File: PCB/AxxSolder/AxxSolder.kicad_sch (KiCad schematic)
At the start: 93 parts, among them IC1 LTC4440AHMS8E-5#PBF, IC2 STM32G431KBT6, IC3 TMP236AQDBZRQ1, IC4 OPA2333AIDRBR, IC5 STM32G431KBT6, IC6 TPS54302DDCR, J1 Conn_01x07_Male, J4 Conn_01x07_Male, Q2 2N7002NXAKR, U1 PEC11L-4220F-S0015, U2 BSC014N04LS

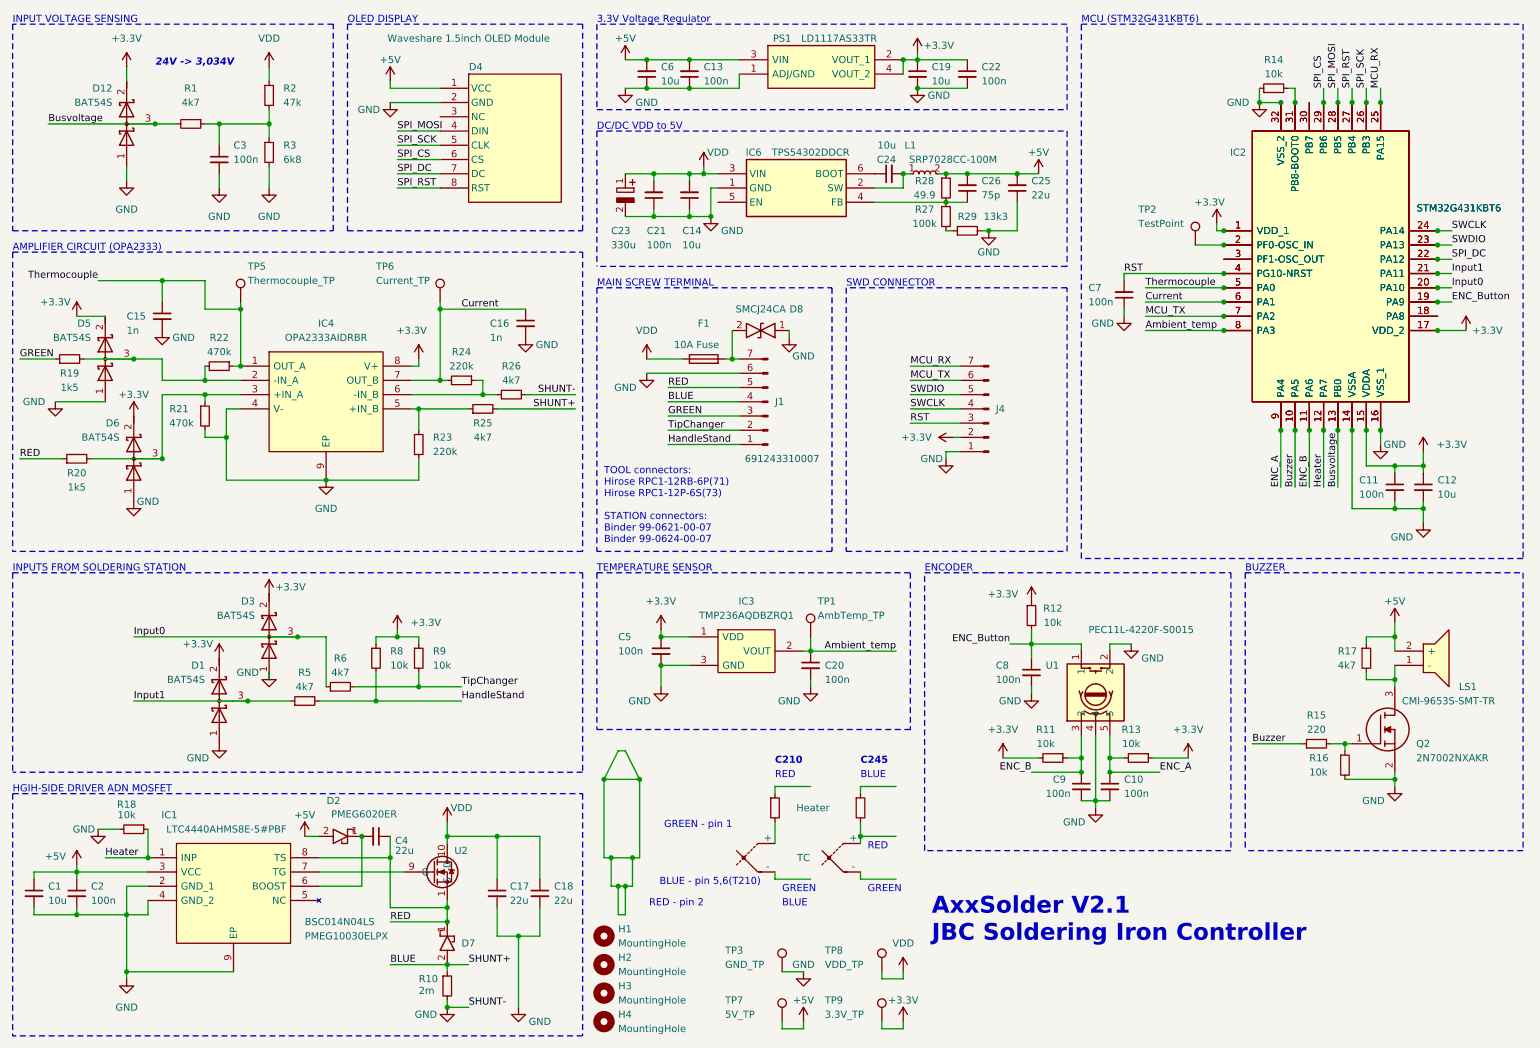
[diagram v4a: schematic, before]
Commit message: Update schematic to reflect new naming of inputs, Stand_inp and Handle_inp
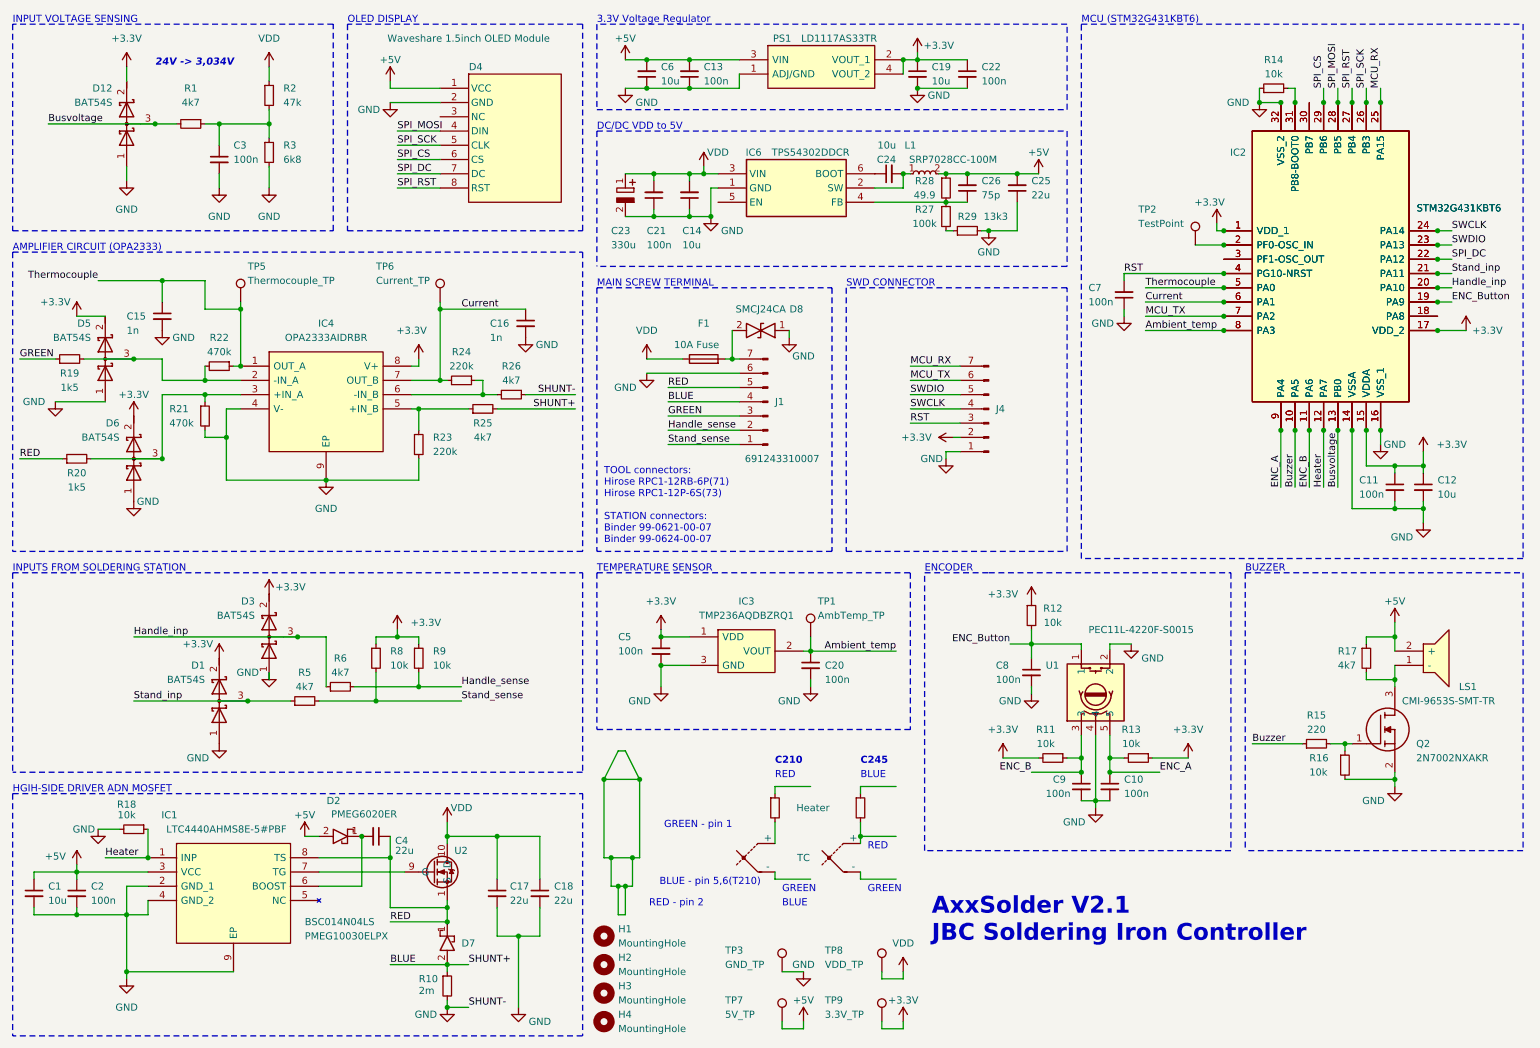
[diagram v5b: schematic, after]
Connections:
- net HandleStand renamed Stand_sense
- net Input0 renamed Handle_inp
- net Input1 renamed Stand_inp
- net TipChanger renamed Handle_sense
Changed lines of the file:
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@@
     (effects (font (size 1.27 1.27)) (justify left bottom))
   )
-  (label "Input0" (at 35.56 125.73 0) (fields_autoplaced)
+  (label "Stand_inp" (at 35.56 137.16 0) (fields_autoplaced)
     (effects (font (size 1.27 1.27)) (justify left bottom))
   )
@@
     (effects (font (size 1.27 1.27)) (justify left bottom))
   )
-  (label "HandleStand" (at 130.81 91.44 0) (fields_autoplaced)
+  (label "Handle_sense" (at 130.81 88.9 0) (fields_autoplaced)
     (effects (font (size 1.27 1.27)) (justify left bottom))
   )
@@
     (effects (font (size 1.27 1.27)) (justify left bottom))
   )
-  (label "Input1" (at 270.51 60.96 0) (fields_autoplaced)
+  (label "Handle_inp" (at 270.51 63.5 0) (fields_autoplaced)
     (effects (font (size 1.27 1.27)) (justify left bottom))
   )
@@
     (effects (font (size 1.27 1.27)) (justify left bottom))
   )
-  (label "TipChanger" (at 130.81 88.9 0) (fields_autoplaced)
+  (label "Stand_sense" (at 130.81 91.44 0) (fields_autoplaced)
     (effects (font (size 1.27 1.27)) (justify left bottom))
   )
@@
     (effects (font (size 1.27 1.27)) (justify left bottom))
   )
-  (label "TipChanger" (at 93.98 134.62 0) (fields_autoplaced)
+  (label "Stand_sense" (at 93.98 137.16 0) (fields_autoplaced)
     (effects (font (size 1.27 1.27)) (justify left bottom))
   )
@@
     (effects (font (size 1.27 1.27)) (justify left bottom))
   )
-  (label "Input1" (at 35.56 137.16 0) (fields_autoplaced)
+  (label "Handle_inp" (at 35.56 125.73 0) (fields_autoplaced)
     (effects (font (size 1.27 1.27)) (justify left bottom))
   )
@@
     (effects (font (size 1.27 1.27)) (justify left bottom))
   )
-  (label "Input0" (at 270.51 63.5 0) (fields_autoplaced)
+  (label "Stand_inp" (at 270.51 60.96 0) (fields_autoplaced)
     (effects (font (size 1.27 1.27)) (justify left bottom))
   )
@@
     (effects (font (size 1.27 1.27)) (justify left bottom))
   )
-  (label "HandleStand" (at 93.98 137.16 0) (fields_autoplaced)
+  (label "Handle_sense" (at 93.98 134.62 0) (fields_autoplaced)
     (effects (font (size 1.27 1.27)) (justify left bottom))
   )

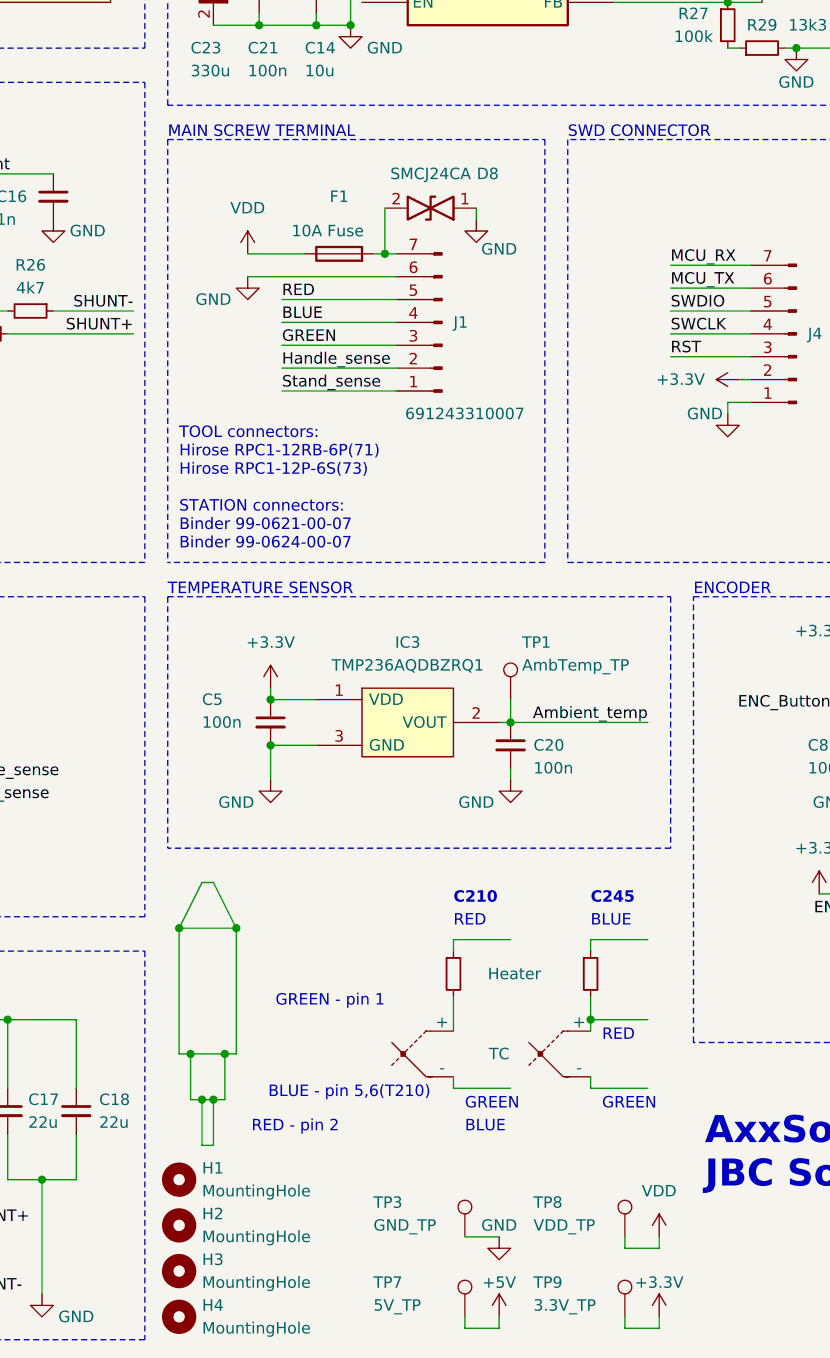
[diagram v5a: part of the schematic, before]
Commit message: Update schematic with proper connections
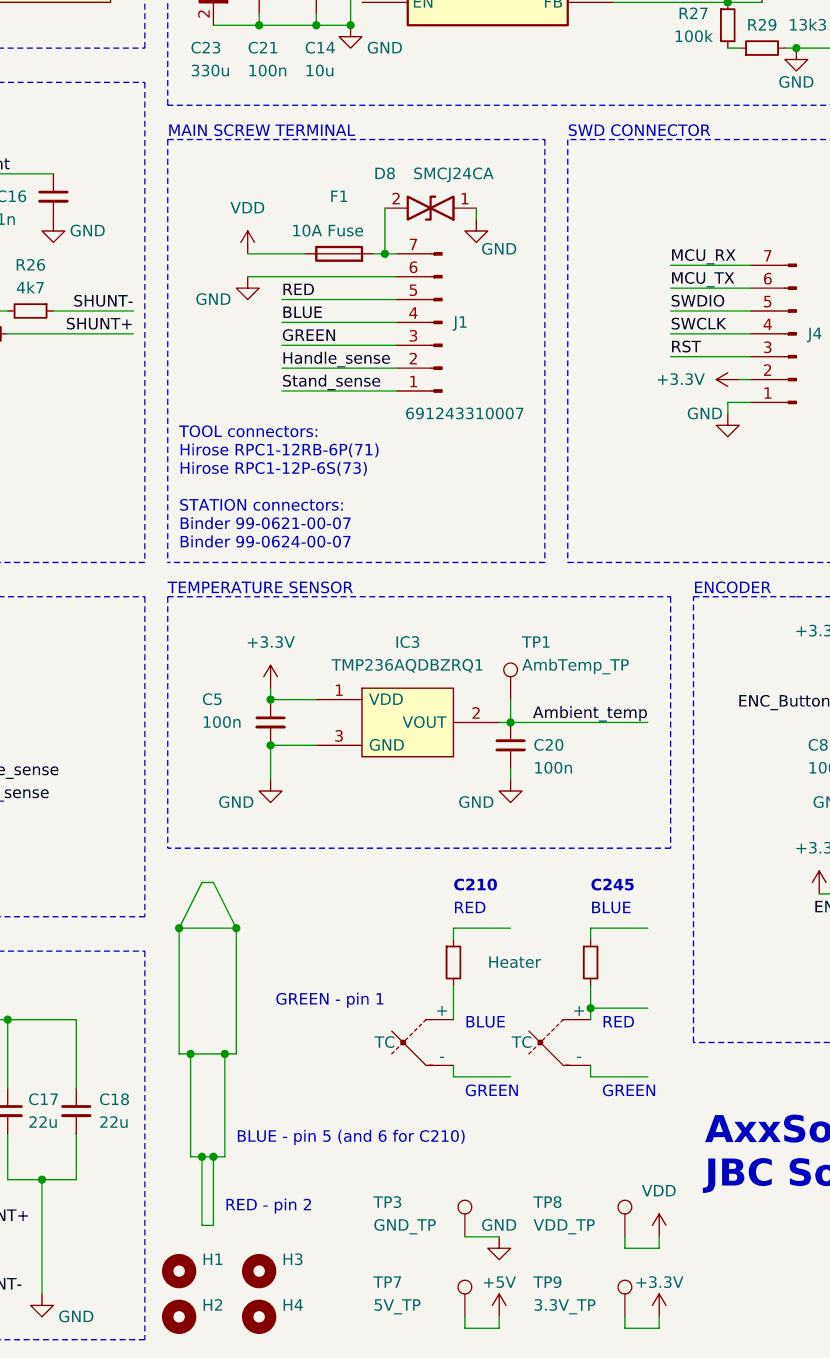
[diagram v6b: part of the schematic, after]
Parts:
- TC2: value Thermocouple -> TC
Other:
- note added: "BLUE - pin 5 (and 6 for C210)"
- note removed: "BLUE - pin 5,6(T210)"
- moved on the sheet: H1, H2, H3, H4

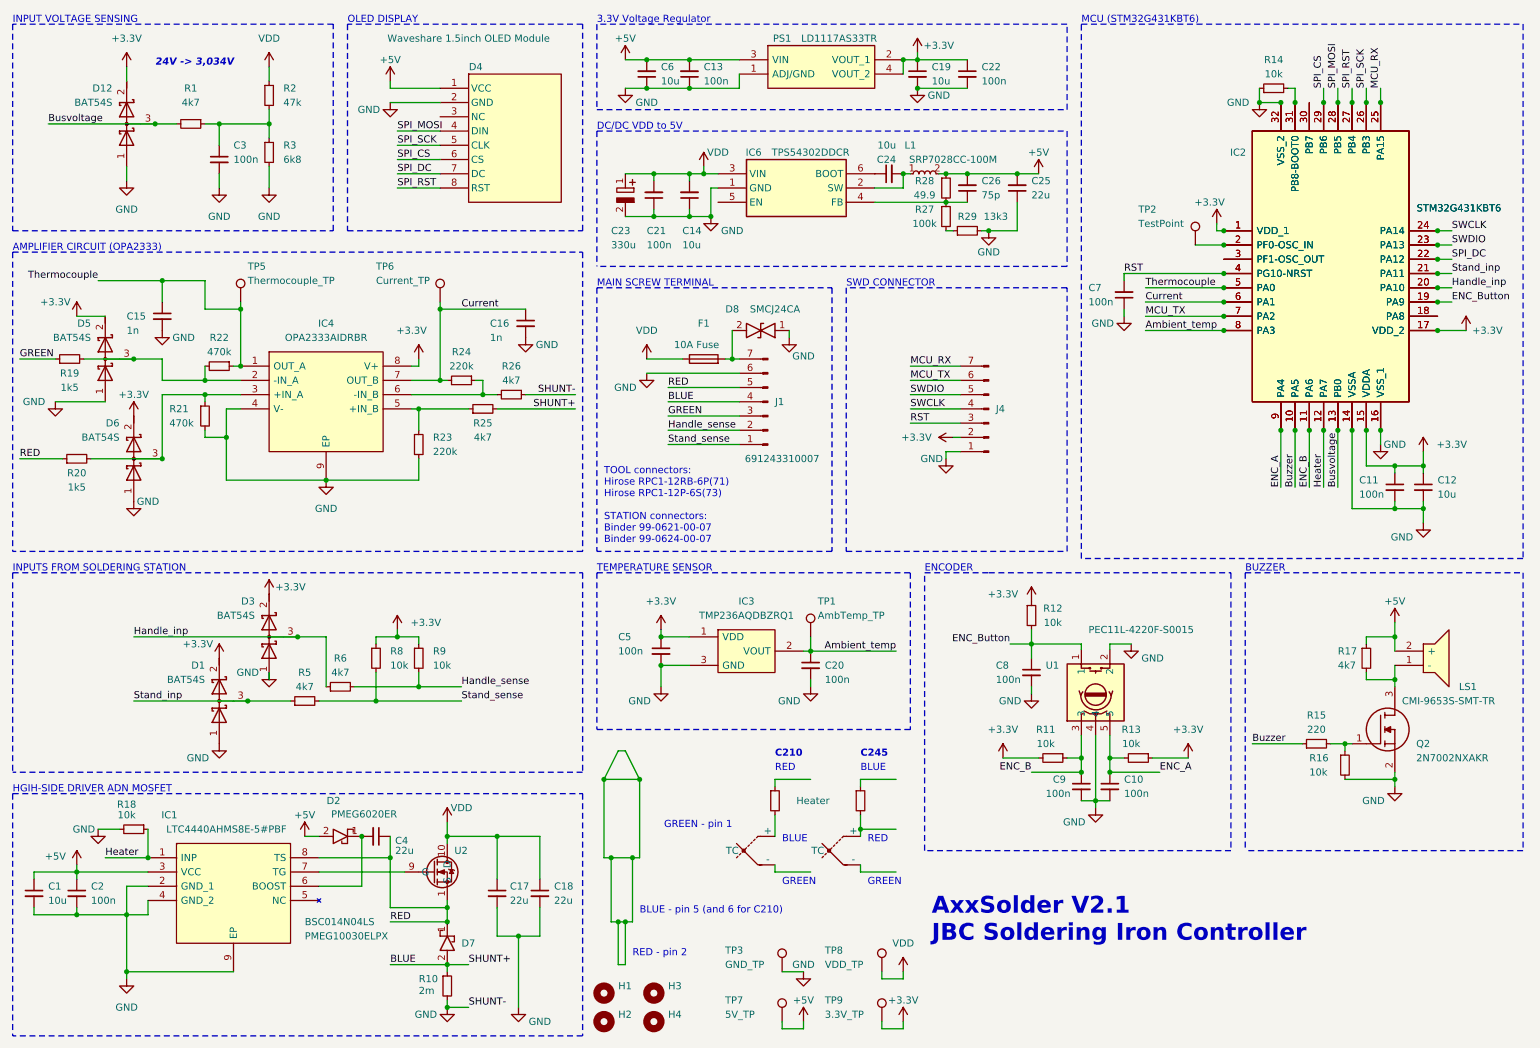
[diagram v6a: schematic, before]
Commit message: Fix output voltage from DC/DC by switching values of R28 and R27. Also change value of C24
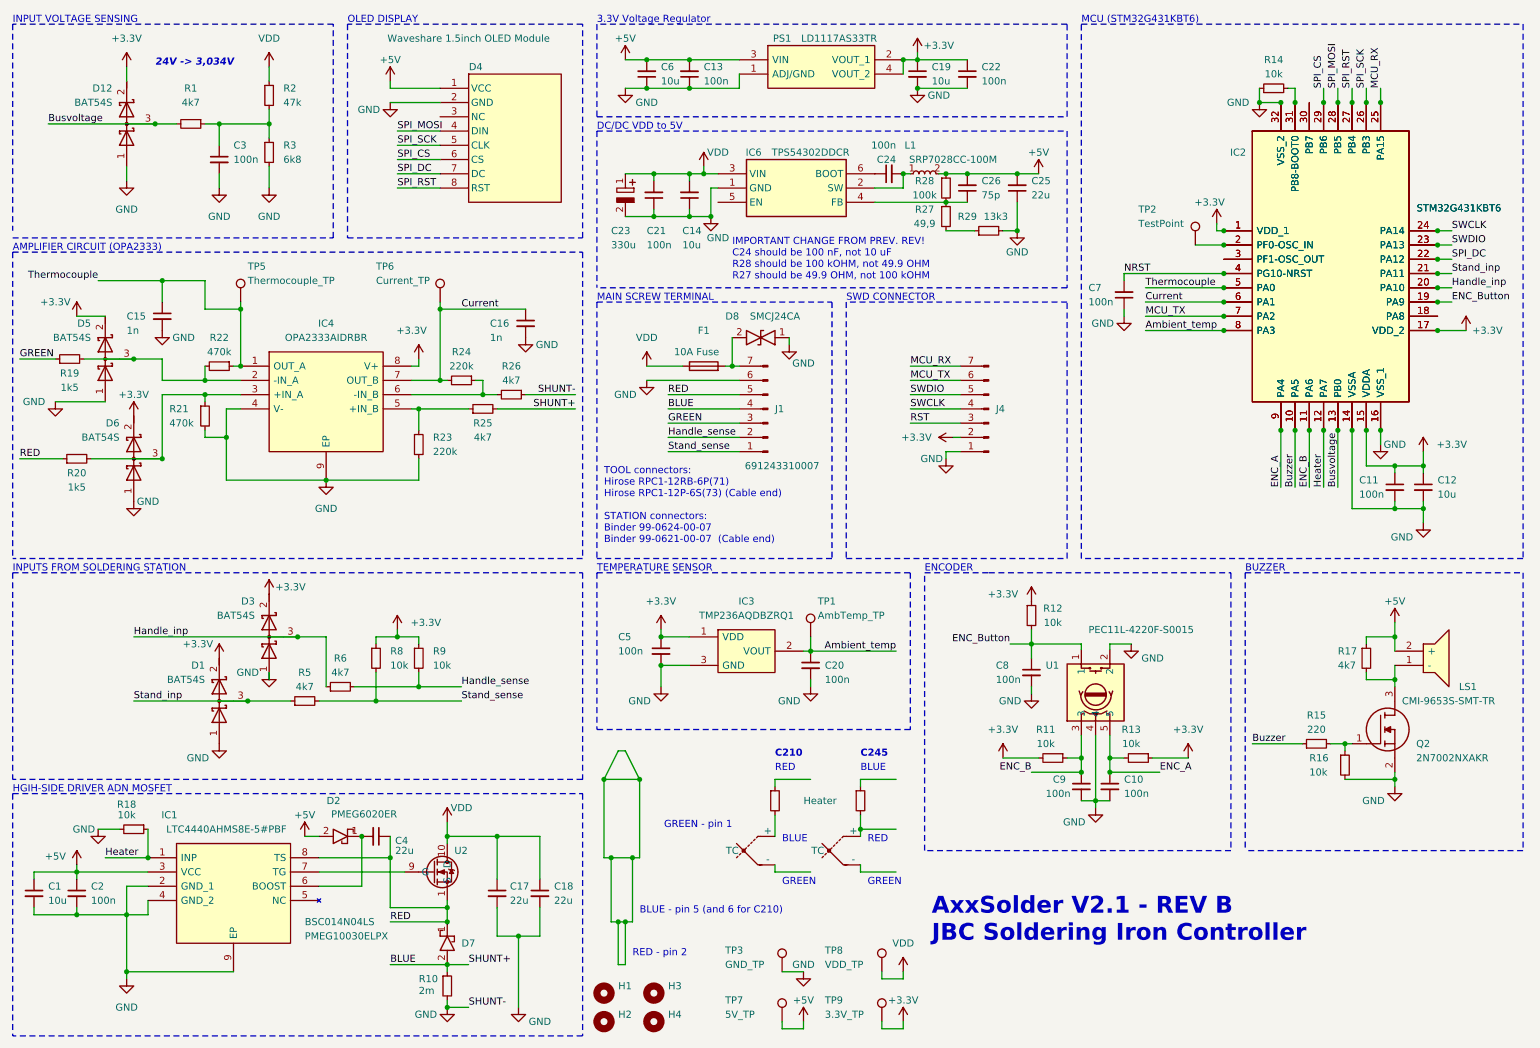
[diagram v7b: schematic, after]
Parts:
- C24: value 10u -> 100n
- R27: value 100k -> 49,9
- R28: value 49.9 -> 100k
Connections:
- net RST: no longer C7.2, IC2.4 (PG10-NRST), IC5.4 (PG10-NRST)
- new net NRST: C7.2, IC2.4 (PG10-NRST), IC5.4 (PG10-NRST)
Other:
- note added: "AxxSolder V2.1 - REV B JBC Soldering Iron Controller"
- note added: "IMPORTANT CHANGE FROM PREV. REV! C24 should be 100 nF, not 10 uF R28 should be 100 kOHM, not 49.9 OHM R27 should be 49.9 OHM, not 100 kOHM"
- note added: "TOOL connectors: Hirose RPC1-12RB-6P(71) Hirose RPC1-12P-6S(73) (Cable end) STATION connectors: Binder 99-0624-00-07 Binder 99-0621-00-07 (Cable end)"
- note removed: "AxxSolder V2.1 JBC Soldering Iron Controller"
- note removed: "TOOL connectors: Hirose RPC1-12RB-6P(71) Hirose RPC1-12P-6S(73) STATION connectors: Binder 99-0621-00-07 Binder 99-0624-00-07"
- moved on the sheet: D8, F1, J1, R29
